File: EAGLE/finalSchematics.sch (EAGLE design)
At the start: 13 parts, among them IC1 STM32F103RBT, P1 DM3CS-SF, Q1 8MHz 131-220

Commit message: Add SD package, fix powers supply of MCU
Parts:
- removed BME280: (no value), pinhead:PINHD-1X4
- removed MINIMU-9: (no value), pinhead:PINHD-1X5
- removed MOD1: GPS, components:L70B-GPS
- removed P1: DM3CS-SF, DM3CS-SF:DM3CS-SF
- removed RADIOANA: (no value), discrete:ANTENNA
- removed U$1: RFM69, RFM69mod:RFM69
- added J1: (no value), SparkFun-Connectors:CONN_02
- added MOD4: GPS, components:L70B-GPS
- added R2, R3: 10k 901-655, rcl:R-EU_R0805
- added RADIOANA1: (no value), discrete:ANTENNA
- added SD1: (no value), components:SD
- added U$2: RFM69, RFM69mod:RFM69
- added U1: LM1117-3.3, SparkFun-IC-Power:V_REG_LM1117SOT223
- IC1: device micro-stm_v3:STM32F103RBT -> components:STM32F103RBT
- MOD2: value (none) -> BME280
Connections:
- removed net CS: IC1MCU.PA10, P1.DAT3
- removed net MISO: IC1MCU.PB14, P1.DAT0
- removed net MOSI: IC1MCU.PB15, P1.CMD
- removed net SCK: IC1MCU.PB13, P1.CLK
- new net N$5: RADIOANA1.1, U$2.ANA
- net +3V3: now also IC1.VDD, IC1.VDDA, MOD2.VIN, MOD3.VDD, R2.2, R3.2, SD1.VDD, U$2.3.3V, U1.OUT, U1.OUT@1; no longer BME280.1, MINIMU-9.5, P1.VDD, U$1.3.3V
- net BOOT0: now also IC1.BOOT0; no longer IC1MCU.BOOT0
- net DIO1_MODEM: now also U$2.DIO1; no longer IC1MCU.PC7, U$1.DIO1
- net GND: now also IC1.VSS, IC1.VSSA, J1.2, MOD2.GND, MOD3.GND, MOD4.GND, SD1.SHILED, SD1.SW1, SD1.SW2, SD1.VSS, U$2.GND@1, U1.ADJ; no longer BME280.2, MINIMU-9.3, MOD1.GND, P1.VSS, U$1.GND@1
- net MISO_MODEM: now also U$2.MISO; no longer U$1.MISO
- net MOSI_MODEM: now also U$2.MOSI; no longer U$1.MOSI
- net N$1: now also C2.2, IC1.OSC_OUT, Q1.1; no longer C1.2, IC1MCU.OSC_IN, Q1.2
- net N$2: now also C1.2, IC1.OSC_IN, Q1.2; no longer C2.2, IC1MCU.OSC_OUT, Q1.1
- net N$3: now also J1.1, U1.IN; no longer RADIOANA.1, U$1.ANA
- net NSS_MODEM: now also U$2.NSS; no longer IC1MCU.PB6, U$1.NSS
- net RX: now also MOD4.RX1; no longer MOD1.RX1
- net SCK_MODEM: now also U$2.SCK; no longer U$1.SCK
- net SCL: now also IC1.PB8, MOD2.SCL, MOD3.SCL, R3.1; no longer BME280.3, IC1MCU.PB8, MINIMU-9.1
- net SDA: now also IC1.PB9, MOD2.SDA, MOD3.SDA, R2.1; no longer BME280.4, IC1MCU.PB9, MINIMU-9.2
- net TX: now also MOD4.TX1; no longer MOD1.TX1

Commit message: Connect modules
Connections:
- removed net DIO1_MODEM: U$2.DIO1
- removed net MISO_MODEM: U$2.MISO
- removed net MOSI_MODEM: U$2.MOSI
- removed net NSS_MODEM: U$2.NSS
- removed net SCK_MODEM: U$2.SCK
- new net CS-RAD: IC1.PA8, U$2.NSS
- new net CS-SD: IC1.PA4, SD1.DAT3
- new net DIO0: IC1.PA11, U$2.DIO0
- new net MISO: IC1.PA6, SD1.DAT0, U$2.MISO
- new net MOSI: IC1.PA7, SD1.CMD, U$2.MOSI
- new net N$6: MOD4.RF_IN
- new net SCK: IC1.PA5, SD1.CLK, U$2.SCK
- net +3V3: now also MOD4.VCC
- net GND: now also U$2.GND@2
- net RX: now also IC1.PA9
- net TX: now also IC1.PA10

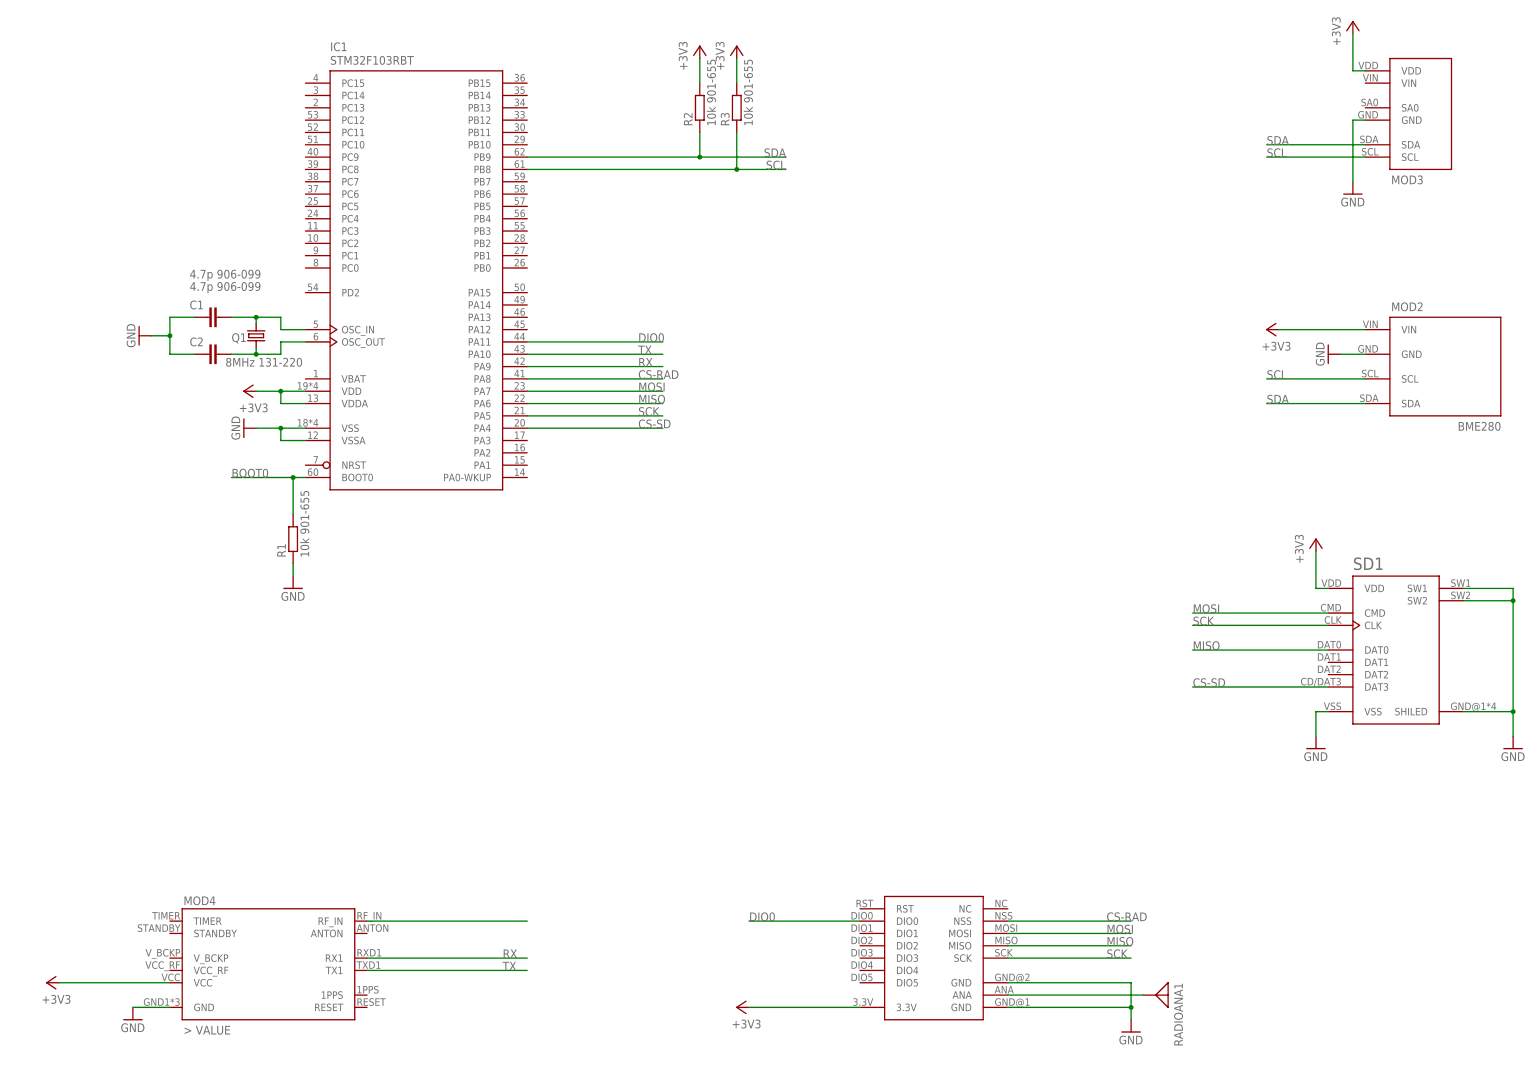
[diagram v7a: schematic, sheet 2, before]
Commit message: Final schematic ready to control
Start creating the board itself
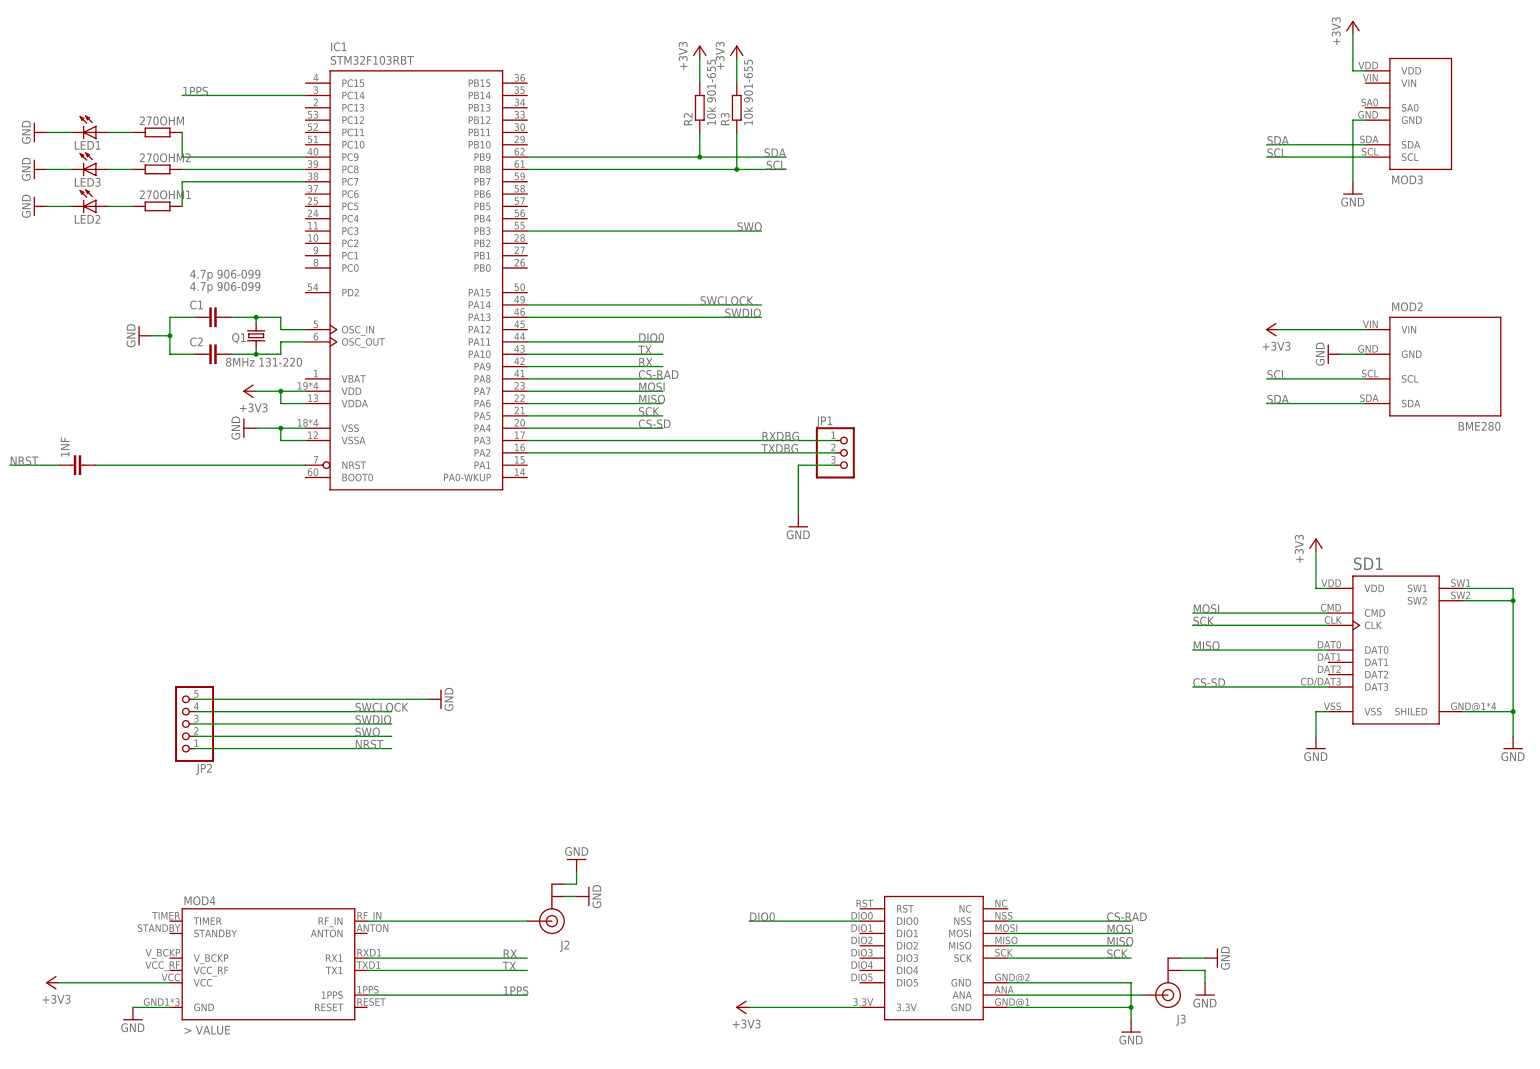
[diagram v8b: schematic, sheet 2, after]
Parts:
- removed R1: 10k 901-655, rcl:R-EU_R0805
- removed RADIOANA1: (no value), discrete:ANTENNA
- added 1NF, C10, C11, C3, C6, C7, C8, C9: (no value), rcl:C-EUC0805
- added 270OHM, 270OHM1, 270OHM2: (no value), resistor:R-EU_R0805
- added C4, C5: 47uF, rcl:CPOL-EU153CLV-0810
- added D1: 1N4004, diode:1N4004
- added J2, J3: U.FL, SparkFun-Connectors:U.FL
- added JP1: (no value), pinhead:PINHD-1X3
- added JP2: (no value), pinhead:PINHD-1X5
- added LED1, LED2, LED3: (no value), led:LEDCHIP-LED0603
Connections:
- removed net BOOT0: IC1.BOOT0, R1.2
- new net 1PPS: IC1.PC14, MOD4.1PPS
- new net N$10: 270OHM.2, IC1.PC9
- new net N$11: 270OHM.1, LED1.A
- new net N$12: 270OHM1.1, LED2.A
- new net N$13: 270OHM2.1, LED3.A
- new net N$4: D1.A, J1.1
- new net N$7: 270OHM1.2, IC1.PC7
- new net N$8: 1NF.2, IC1.NRST
- new net N$9: 270OHM2.2, IC1.PC8
- new net NRST: 1NF.1, JP2.1
- new net RXDBG: IC1.PA3, JP1.1
- new net SWCLOCK: IC1.PA14, JP2.4
- new net SWDIO: IC1.PA13, JP2.3
- new net SWO: IC1.PB3, JP2.2
- new net TXDBG: IC1.PA2, JP1.2
- net +3V3: now also C10.1, C11.1, C3.1, C5.+, C6.1, C7.1, C8.1, C9.1
- net GND: now also C10.2, C11.2, C3.2, C4.-, C5.-, C6.2, C7.2, C8.2, C9.2, J2.GND@0, J2.GND@1, J3.GND@0, J3.GND@1, JP1.3, JP2.5, LED1.C, LED2.C, LED3.C; no longer R1.1
- net N$3: now also C4.+, D1.C; no longer J1.1
- net N$5: now also J3.SIGNAL; no longer RADIOANA1.1
- net N$6: now also J2.SIGNAL
